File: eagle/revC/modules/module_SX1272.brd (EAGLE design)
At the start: 24.1 x 32.8 mm, 18 parts, among them X1 734120110

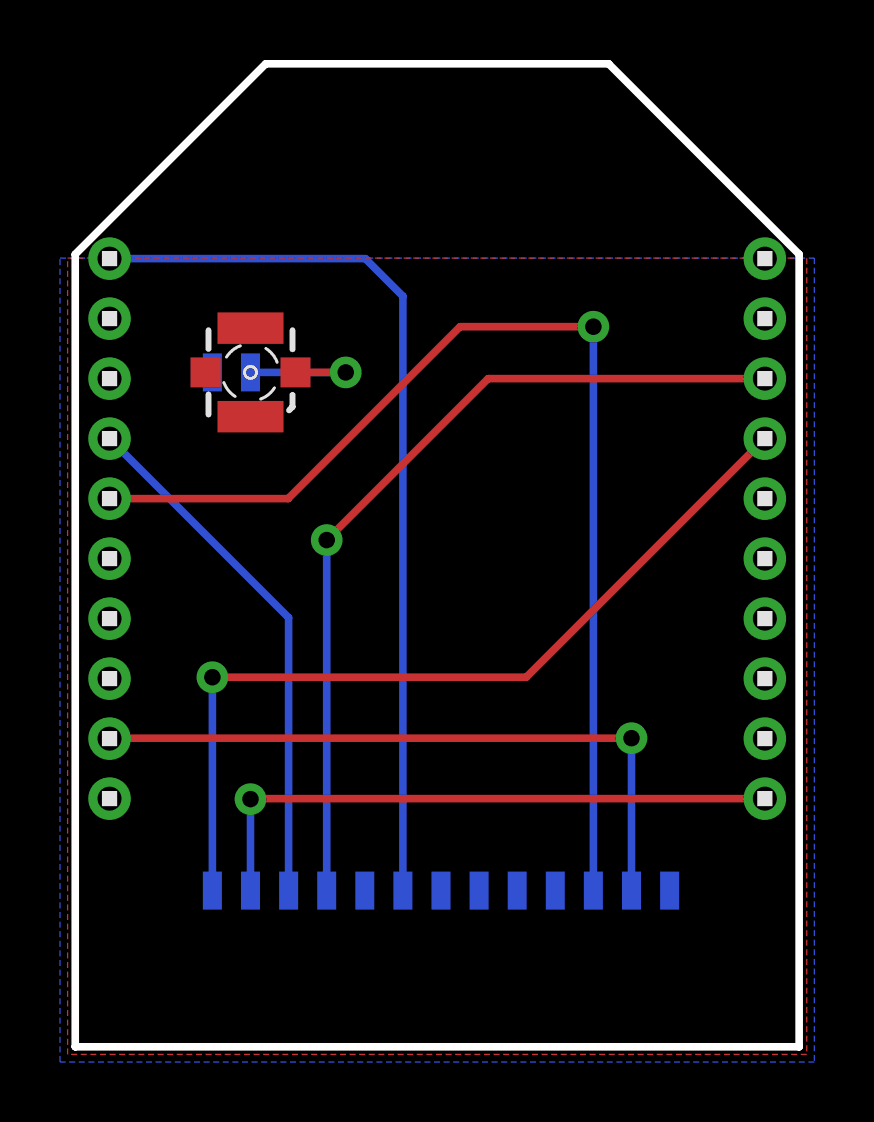
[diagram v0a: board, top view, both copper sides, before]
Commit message: Replaced modules with library parts
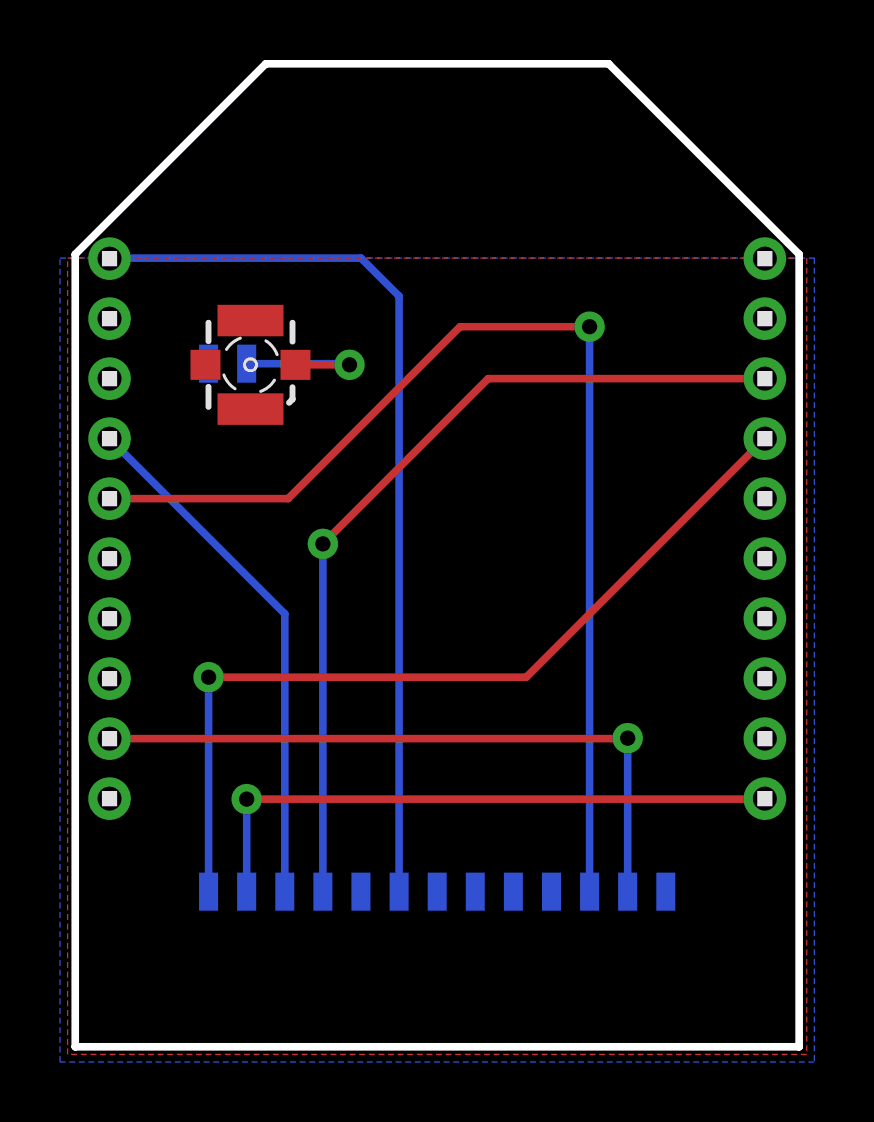
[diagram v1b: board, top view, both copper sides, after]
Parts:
- removed 3.3V, ANT, DIO0, DIO1, DIO2, DIO3, DIO4, DIO5, GND, GND_ANT, MISO, MOSI, NSS, RESET, SCK: (no value), wirepad:SMD0,65-1,27
- added U$1: SX1272, RadioShield:SX1272
- moved X1 0.25 mm to (5.97, 22.9)
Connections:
- removed net ANT: ANT.1, X1.1
- removed net INT0: DIO0.1, LEFT1.9
- removed net INT1: DIO1.1, LEFT1.5
- removed net SPI_CS: NSS.1, RIGHT1.4
- removed net SPI_MISO: LEFT1.4, MISO.1
- removed net SPI_MOSI: MOSI.1, RIGHT1.10
- removed net SPI_SCK: RIGHT1.3, SCK.1
- new net N$2: U$1.ANT, X1.1
- new net N$3: LEFT1.9, U$1.DIO0
- new net N$4: RIGHT1.10, U$1.MOSI
- new net N$5: RIGHT1.4, U$1.NSS
- new net N$6: RIGHT1.3, U$1.SCK
- new net N$7: LEFT1.5, U$1.DIO1
- new net N$8: LEFT1.4, U$1.MISO
- net GND: now also U$1.GND@1, U$1.GND@2; no longer GND.1, GND_ANT.1
- net VCC: now also U$1.3.3V; no longer 3.3V.1
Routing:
- net INT1: track 37.3 -> 0.00 mm, vias 1 -> 0
- net N$7: track 0.00 -> 37.2 mm, vias 0 -> 1
- net N$5: track 0.00 -> 29.0 mm, vias 0 -> 1
- net SPI_CS: track 28.8 -> 0.00 mm, vias 1 -> 0
- net N$6: track 0.00 -> 28.6 mm, vias 0 -> 1
- net SPI_SCK: track 28.5 -> 0.00 mm, vias 1 -> 0
- net INT0: track 22.5 -> 0.00 mm, vias 1 -> 0
- net N$3: track 0.00 -> 22.4 mm, vias 0 -> 1
- net N$4: track 0.00 -> 20.4 mm, vias 0 -> 1
- net SPI_MOSI: track 20.2 -> 0.00 mm, vias 1 -> 0
- net SPI_MISO: track 17.5 -> 0.00 mm
- net N$8: track 0.00 -> 17.5 mm
- net N$2: track 0.00 -> 5.25 mm, vias 0 -> 1
- net ANT: track 4.85 -> 0.00 mm, vias 1 -> 0
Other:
- board text removed: "3.3V"
- board text removed: "ANT"
- board text removed: "DIO0"
- board text removed: "DIO1"
- board text removed: "DIO2"
- board text removed: "DIO3"
- board text removed: "DIO4"
- board text removed: "DIO5"
- board text removed: "GND"
- board text removed: "MISO"
- board text removed: "MOSI"
- board text removed: "NSS"
- board text removed: "RESET"
- board text removed: "SCK"

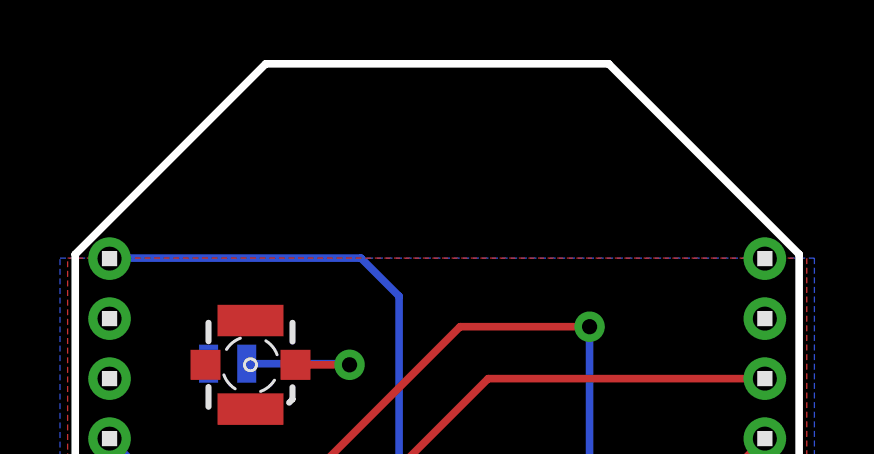
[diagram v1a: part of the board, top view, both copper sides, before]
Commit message: Fixed module name layers
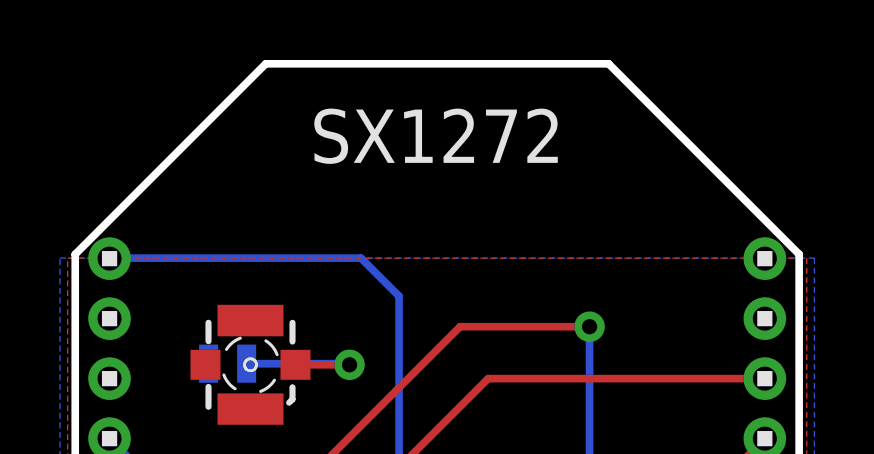
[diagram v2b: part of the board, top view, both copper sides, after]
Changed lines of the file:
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@@
 <wire x1="24.257" y1="26.543" x2="24.257" y2="0.127" width="0.254" layer="20"/>
 <wire x1="24.257" y1="0.127" x2="0.127" y2="0.127" width="0.254" layer="20"/>
-<text x="12.192" y="30.48" size="1.778" layer="51" ratio="15" rot="SR0" align="center">SX1272</text>
+<text x="12.192" y="30.48" size="1.778" layer="25" ratio="15" rot="SR0" align="center">SX1272</text>
 </plain>
 <attributes>
